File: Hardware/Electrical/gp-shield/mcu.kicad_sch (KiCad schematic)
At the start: 87 parts, among them J3 Conn_01x04, Q3 Q_NMOS_GDS, SW2 SW_Push, SW3 SW_Push

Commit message: Removed net ties from BOM
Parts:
- NT1, NT10, NT2, NT3, NT4, NT5, NT6, NT7, NT8, NT9: now left out of the parts list
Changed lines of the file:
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@@
   )
   (symbol (lib_id "Device:NetTie_2") (at 44.45 111.76 90) (unit 1)
-    (in_bom yes) (on_board yes) (fields_autoplaced)
+    (in_bom no) (on_board yes) (fields_autoplaced)
     (property "Reference" "NT1" (id 0) (at 45.72 110.4899 90)
       (effects (font (size 1.27 1.27)) (justify right) hide)
@@
   )
   (symbol (lib_id "Device:NetTie_2") (at 62.23 140.97 90) (unit 1)
-    (in_bom yes) (on_board yes) (fields_autoplaced)
+    (in_bom no) (on_board yes) (fields_autoplaced)
     (property "Reference" "NT7" (id 0) (at 63.5 139.6999 90)
       (effects (font (size 1.27 1.27)) (justify right) hide)
@@
   )
   (symbol (lib_id "Device:NetTie_2") (at 46.99 111.76 90) (unit 1)
-    (in_bom yes) (on_board yes) (fields_autoplaced)
+    (in_bom no) (on_board yes) (fields_autoplaced)
     (property "Reference" "NT3" (id 0) (at 48.26 110.4899 90)
       (effects (font (size 1.27 1.27)) (justify right) hide)
@@
   )
   (symbol (lib_id "Device:NetTie_2") (at 49.53 83.82 90) (unit 1)
-    (in_bom yes) (on_board yes) (fields_autoplaced)
+    (in_bom no) (on_board yes) (fields_autoplaced)
     (property "Reference" "NT4" (id 0) (at 50.8 82.5499 90)
       (effects (font (size 1.27 1.27)) (justify right) hide)
@@
   )
   (symbol (lib_id "Device:NetTie_2") (at 46.99 83.82 90) (unit 1)
-    (in_bom yes) (on_board yes) (fields_autoplaced)
+    (in_bom no) (on_board yes) (fields_autoplaced)
     (property "Reference" "NT2" (id 0) (at 48.26 82.5499 90)
       (effects (font (size 1.27 1.27)) (justify right) hide)
@@
   )
   (symbol (lib_id "Device:NetTie_2") (at 59.69 140.97 90) (unit 1)
-    (in_bom yes) (on_board yes) (fields_autoplaced)
+    (in_bom no) (on_board yes) (fields_autoplaced)
     (property "Reference" "NT6" (id 0) (at 60.96 139.6999 90)
       (effects (font (size 1.27 1.27)) (justify right) hide)
@@
   )
   (symbol (lib_id "Device:NetTie_2") (at 49.53 111.76 90) (unit 1)
-    (in_bom yes) (on_board yes) (fields_autoplaced)
+    (in_bom no) (on_board yes) (fields_autoplaced)
     (property "Reference" "NT5" (id 0) (at 50.8 110.4899 90)
       (effects (font (size 1.27 1.27)) (justify right) hide)
@@
   )
   (symbol (lib_id "Device:NetTie_2") (at 64.77 140.97 90) (unit 1)
-    (in_bom yes) (on_board yes) (fields_autoplaced)
+    (in_bom no) (on_board yes) (fields_autoplaced)
     (property "Reference" "NT8" (id 0) (at 66.04 139.6999 90)
       (effects (font (size 1.27 1.27)) (justify right) hide)
@@
   )
   (symbol (lib_id "Device:NetTie_2") (at 243.84 124.46 90) (unit 1)
-    (in_bom yes) (on_board yes) (fields_autoplaced)
+    (in_bom no) (on_board yes) (fields_autoplaced)
     (property "Reference" "NT10" (id 0) (at 245.11 123.1899 90)
       (effects (font (size 1.27 1.27)) (justify right) hide)
@@
   )
   (symbol (lib_id "Device:NetTie_2") (at 241.3 124.46 90) (unit 1)
-    (in_bom yes) (on_board yes) (fields_autoplaced)
+    (in_bom no) (on_board yes) (fields_autoplaced)
     (property "Reference" "NT9" (id 0) (at 242.57 123.1899 90)
       (effects (font (size 1.27 1.27)) (justify right) hide)

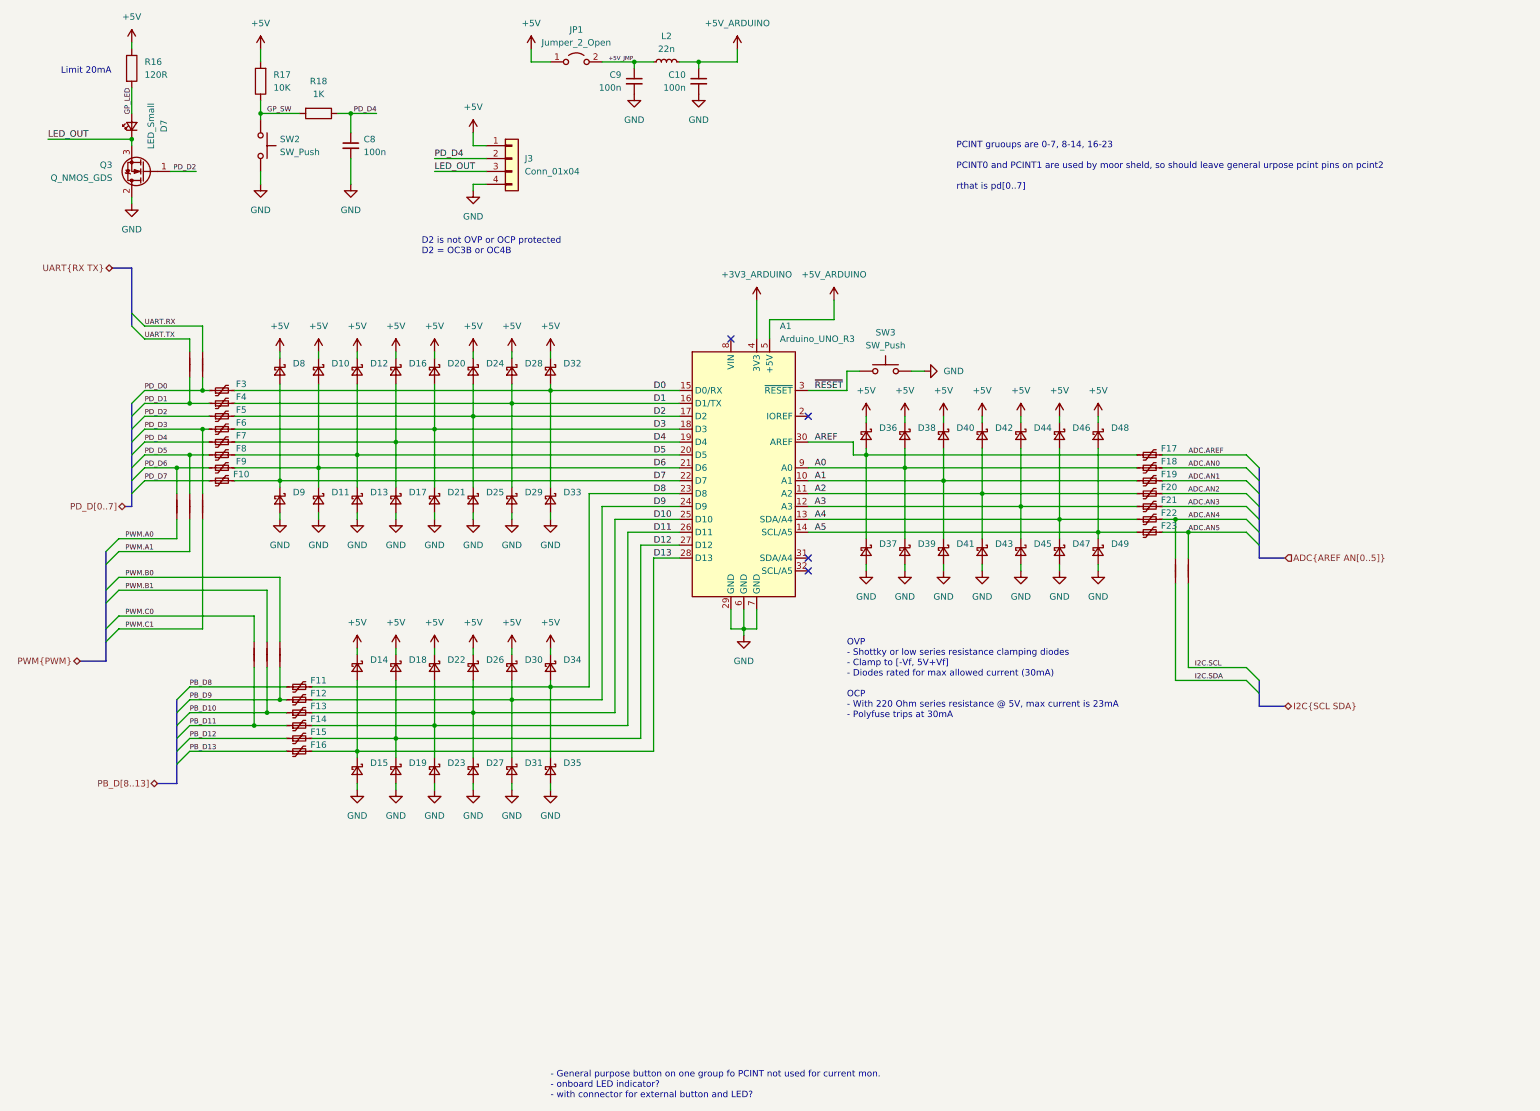
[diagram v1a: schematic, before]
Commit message: Minor cosmetic imporvements
title block and colour theme
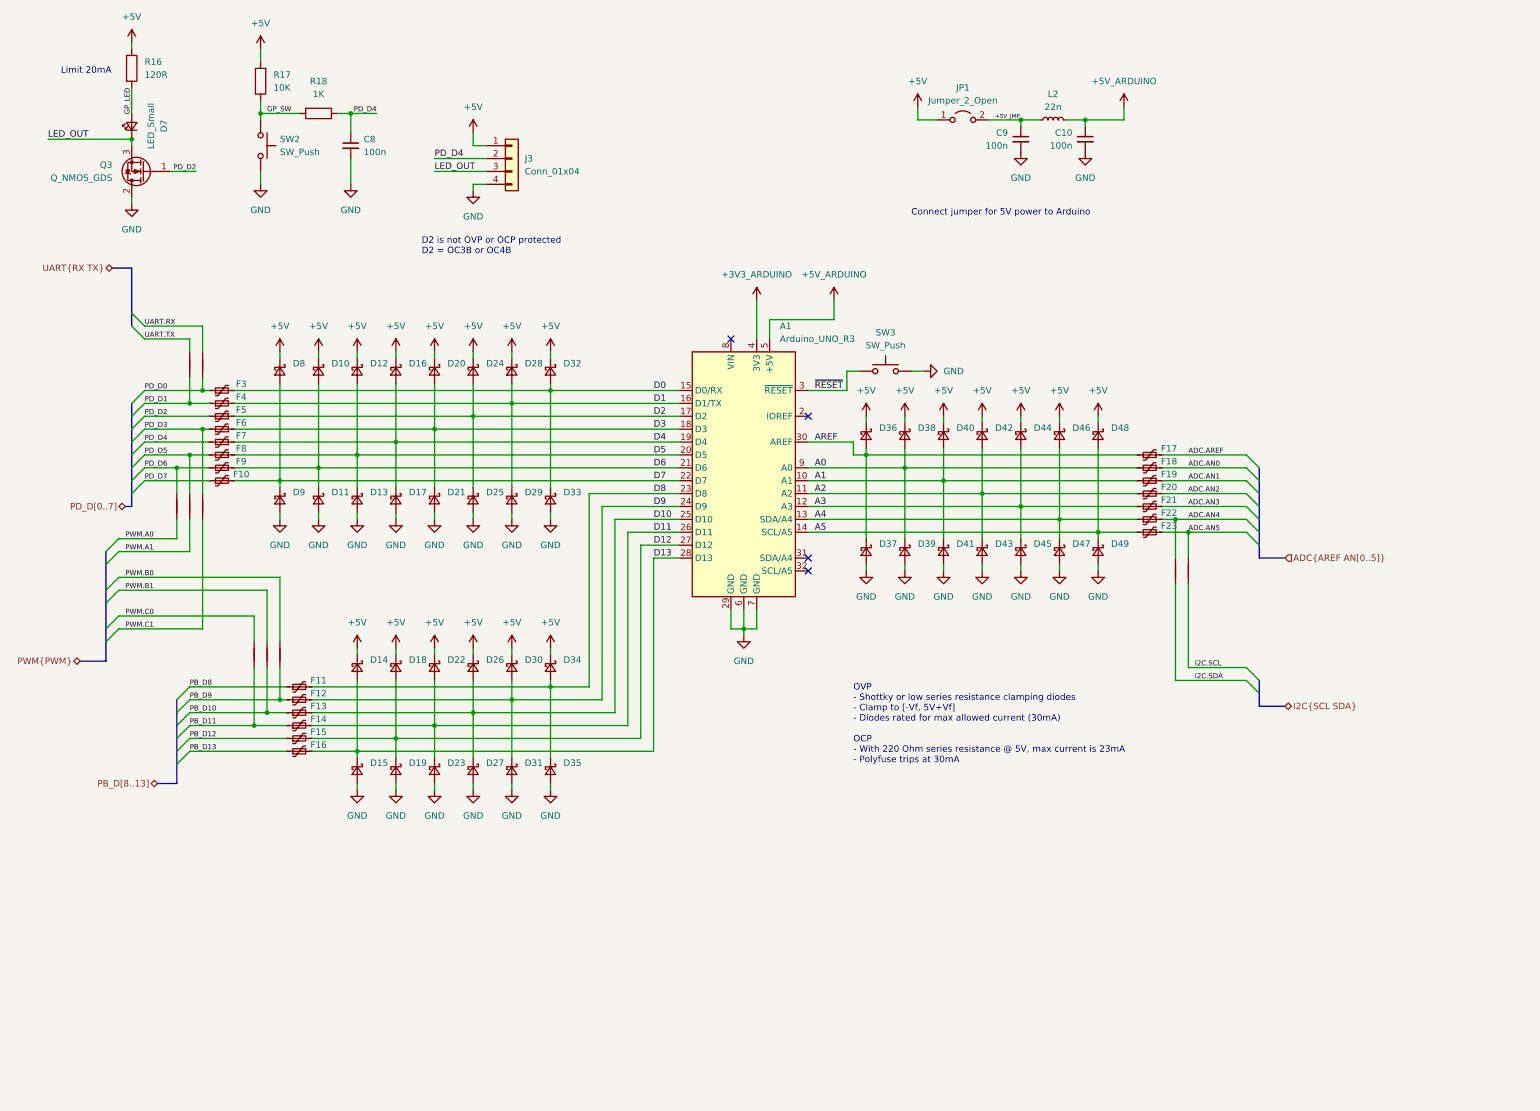
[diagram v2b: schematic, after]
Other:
- note added: "Connect jumper for 5V power to Arduino"
- note removed: "- General purpose button on one group fo PCINT not used for current mon. - onboard LED indicator? - with connector for external button and LED?"
- note removed: "PCINT gruoups are 0-7, 8-14, 16-23 PCINT0 and PCINT1 are used by moor sheld, so should leave general urpose pcint pins on pcint2 rthat is pd[0..7]"
- company: (none) -> University of Tasmania
- title: (none) -> gp-shield MCU
- moved on the sheet: C10, C9, JP1, L2

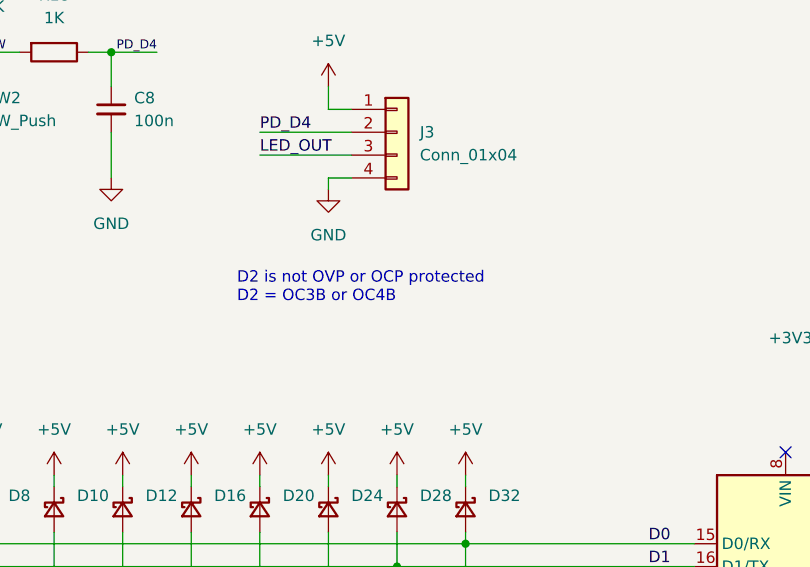
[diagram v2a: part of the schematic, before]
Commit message: Minor tweaks to annotation
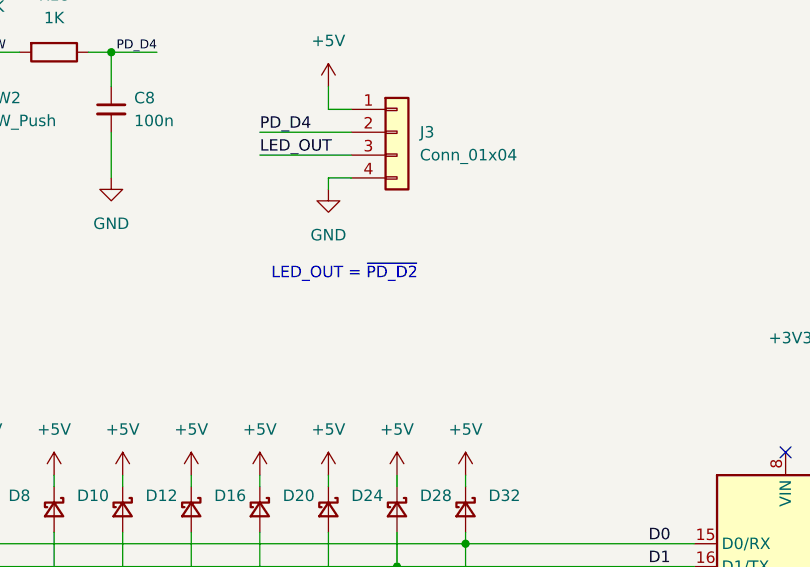
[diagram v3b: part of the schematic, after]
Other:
- note added: "LED_OUT = ~{PD_D2}"
- note removed: "D2 is not OVP or OCP protected D2 = OC3B or OC4B"
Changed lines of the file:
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@@
     (stroke (width 0) (type default) (color 0 0 0 0))
   )
-  (text "D2 is not OVP or OCP protected\nD2 = OC3B or OC4B\n" (at 92.71 62.23 0)
+  (text "LED_OUT = ~{PD_D2}" (at 96.52 59.69 0)
     (effects (font (size 1.27 1.27)) (justify left bottom))
   )
